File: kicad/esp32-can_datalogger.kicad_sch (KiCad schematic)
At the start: 46 parts, among them J1 USB_C_Receptacle_USB2.0_16P, J2 USB_C_Receptacle_USB2.0_16P, J3 USB_C_Receptacle_USB2.0_16P, J6 USB_C_Receptacle_USB2.0_16P, J7 Conn_Coaxial, J8 MicroSD, J9 Conn_01x04_Socket, SW1 SW_Push, SW2 SW_Push, U2 PA1616D, U3 PI4ULS3V204LEX, U4 AZ1117-1.8, U5 TJA1051T, U6 TJA1051T, U7 ICM-20948

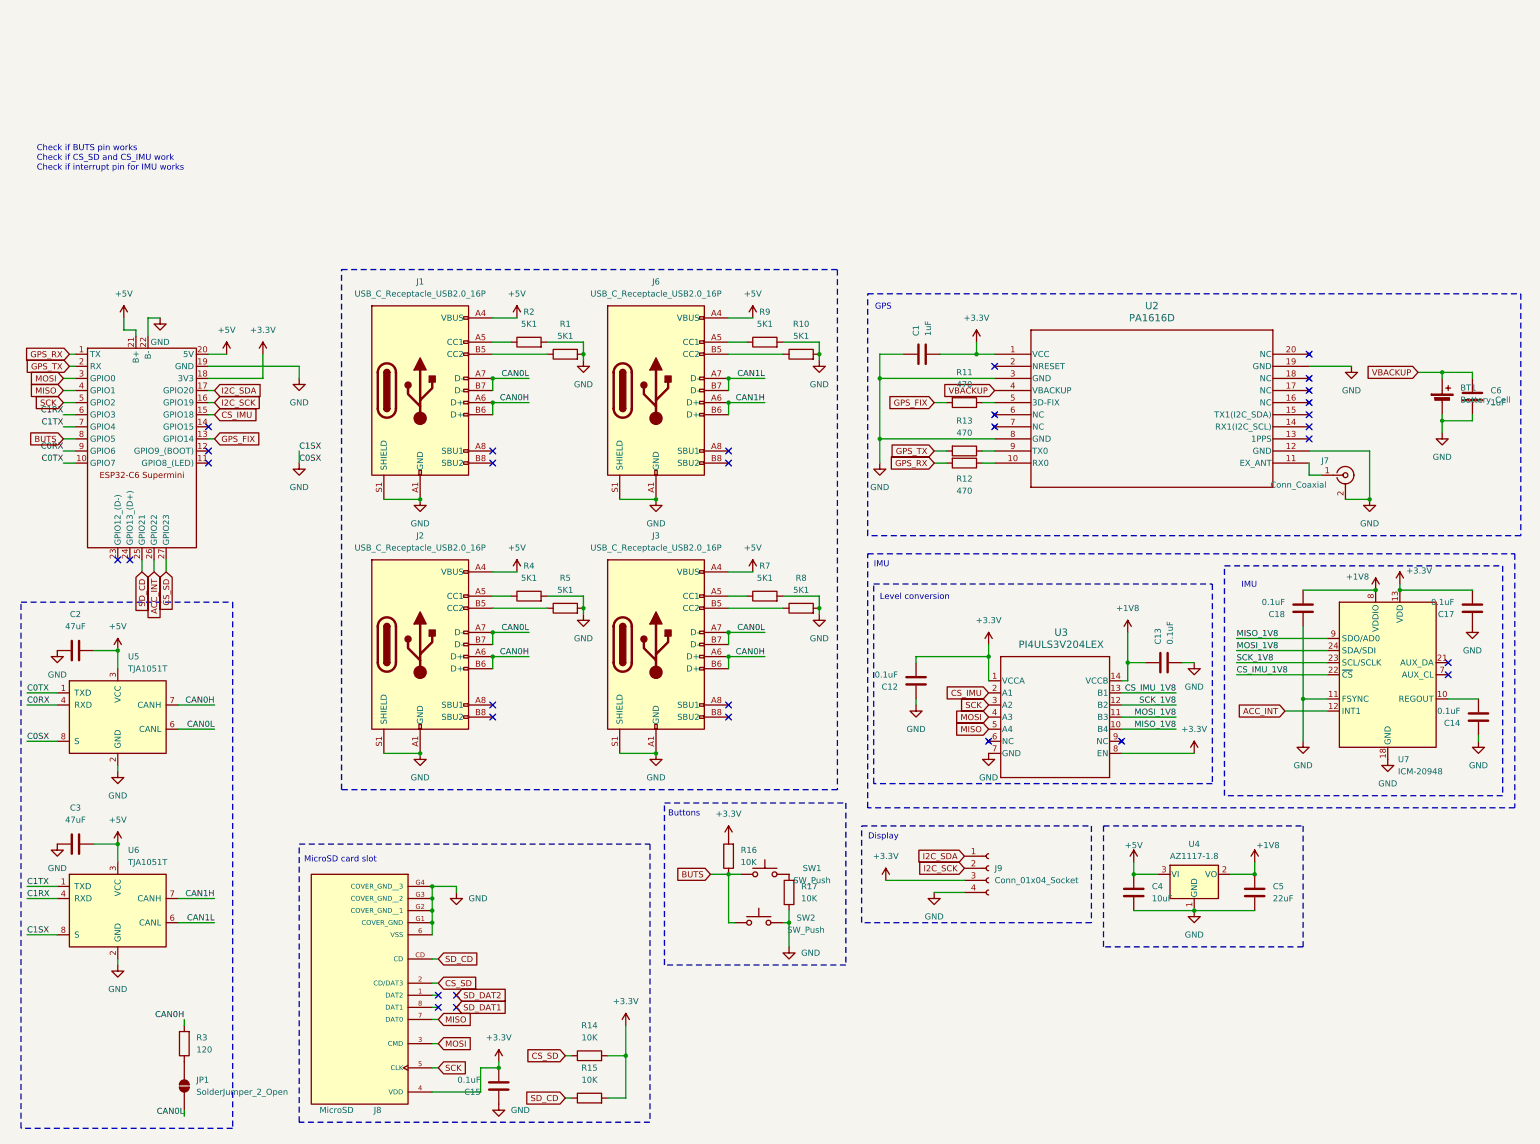
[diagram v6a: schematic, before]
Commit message: cleanup schematic for ss
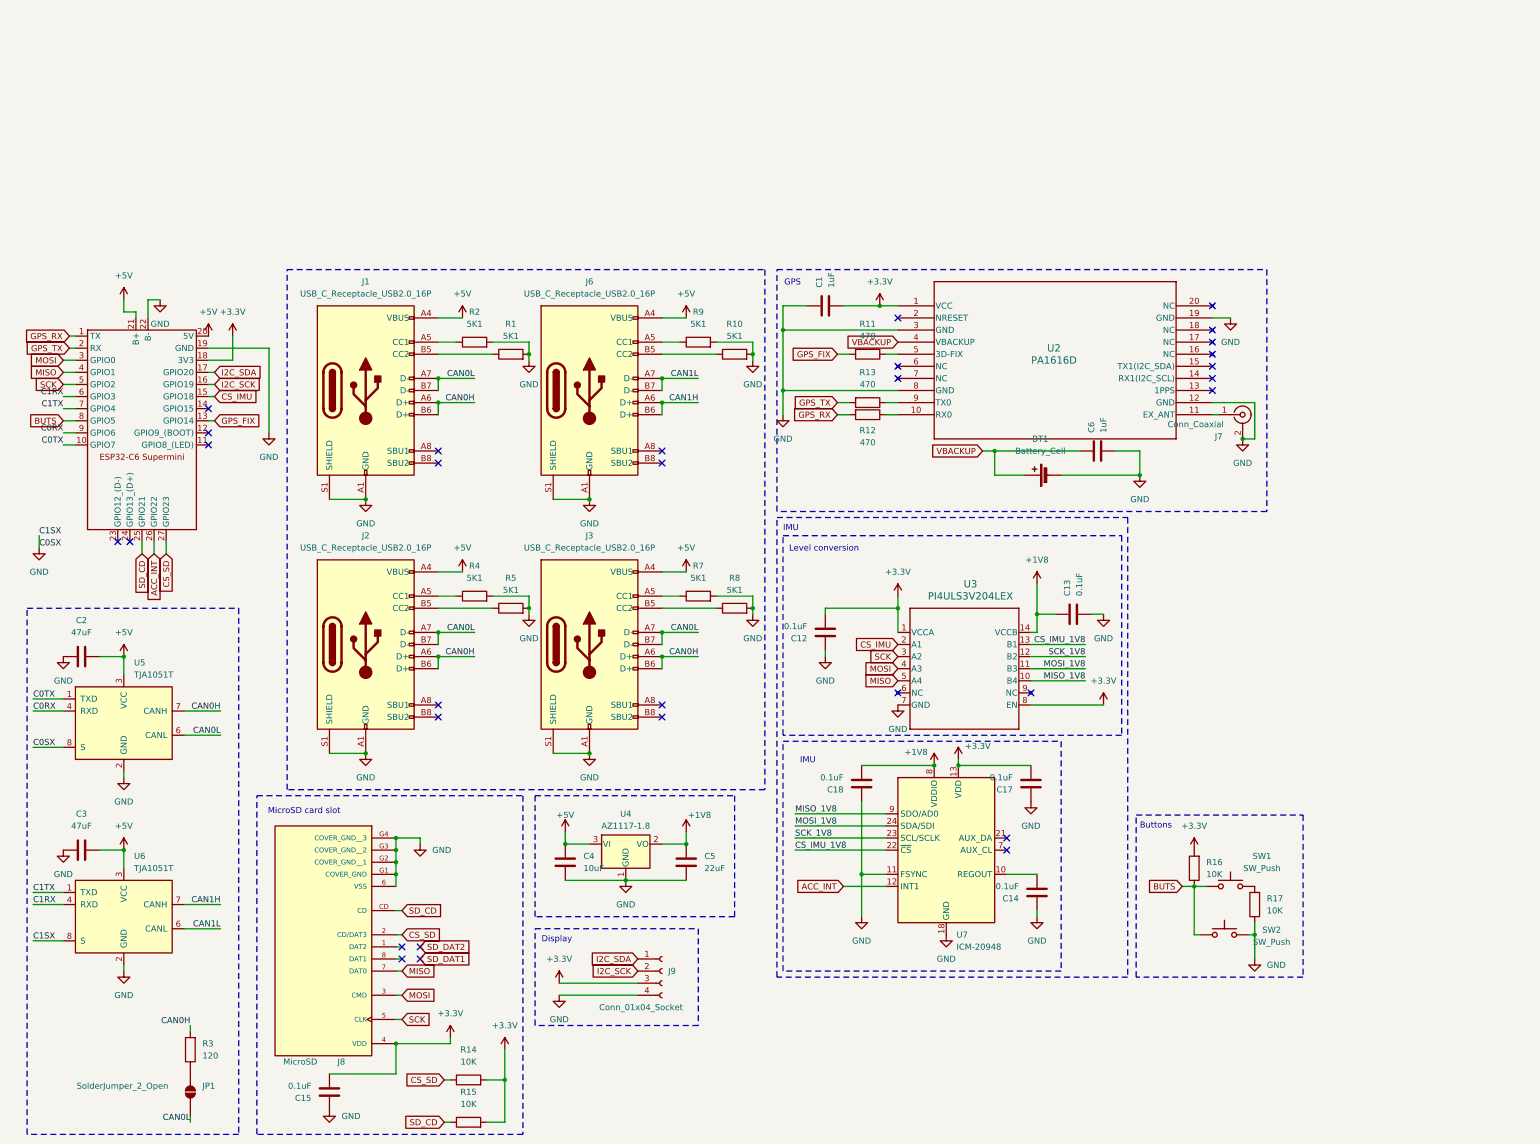
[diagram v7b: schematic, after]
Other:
- note removed: "Check if BUTS pin works Check if CS_SD and CS_IMU work Check if interrupt pin for IMU works"
- moved on the sheet: BT1, C1, C12, C13, C14, C15, C17, C18, C2, C3, C4, C5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
